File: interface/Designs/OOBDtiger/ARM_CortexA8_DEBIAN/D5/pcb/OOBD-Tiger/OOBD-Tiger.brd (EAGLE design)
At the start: 63.4 x 38.2 mm, 83 parts, among them IC4 DS3231, U1 SY6280, U10 MP1482DS, U2 SN65HVD230(SO8), U6 SN65HVD230(SO8)

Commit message: modify USB-OTG and USB-Host interface
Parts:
- added C2: 100nF, rcl:C0603
- added R19: 6k8k/1%, rcl:R0603
- added R21: 10k, rcl:R0603
- added R22: 2.2k/1%, rcl:R0603
- added R23: NA, rcl:R0603
- added R24: 10k/1%, rcl:R0603
- added U3: SY6280, OLIMEX_IC:SOT23-5
- renumbered USB_HOST2 to USB_HOST
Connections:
- net USB0-DRV renamed USB0_DRV
- net USB0-ID renamed USB0_ID
- net USB0-VBUS renamed USB0_VBUS
- removed net USB1_DM1: USB_HOST.2
- removed net USB1_DP1: USB_HOST.3
- removed net USB1_VBUS1: C10.1, C8.1, L5.1
- new net N$13: C10.1, C8.1, L5.1, R22.2, U3.1
- new net N$3: R19.2, U3.3
- net +5V: now also C2.1, U3.5
- net GND: now also C2.2, R19.1, R21.1, R24.1, U3.2
- net USB1_CE: now also R23.2
- net USB1_DM: now also USB_HOST.2
- net USB1_DP: now also USB_HOST.3
- net USB1_DRV: now also R21.2, R23.1, U3.4
- net USB1_ID: now also R24.2
- net USB1_VBUS: now also R22.1
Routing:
- net USB1_VBUS1: track 10.1 -> 0.00 mm, vias 2 -> 0
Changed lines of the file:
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@@
 <?xml version="1.0" encoding="utf-8"?>
 <!DOCTYPE eagle SYSTEM "eagle.dtd">
-<eagle version="7.6.0">
+<eagle version="6.4">
 <drawing>
 <settings>
@@
 <pass name="Default">
 <param name="RoutingGrid" value="50mil"/>
-<param name="AutoGrid" value="1"/>
-<param name="Efforts" value="0"/>
-<param name="TopRouterVariant" value="1"/>
 <param name="tpViaShape" value="round"/>
 <param name="PrefDir.1" value="|"/>
@@
 <element name="IC4" library="DS3231_industrialberry" package="SOIC-16W" value="DS3231" x="16.129" y="16.002" rot="R270"/>
 <element name="BAT2" library="SparkFun" package="BATTCON_12MM_PTH" value="" x="21.844" y="31.623"/>
-<element name="USB_HOST2" library="OLIMEX_CONNECTORS" package="USB_PN87520_DEV_PTH" value="USB_A_VERTICAL" x="2.159" y="16.129" rot="R270"/>
+<element name="USB_HOST" library="OLIMEX_CONNECTORS" package="USB_PN87520_DEV_PTH" value="USB_A_VERTICAL" x="2.159" y="16.129" rot="R270"/>
 <element name="L5" library="rcl" package="L0805_5MIL_DWS" value="FB0805/600R/2A" x="25.4" y="12.319" smashed="yes">
 <attribute name="NAME" x="27.305" y="11.811" size="1.27" layer="25" ratio="20"/>
@@
 <element name="MS-CAN" library="SparkFun" package="SJ_2S-NO" value="OPEN" x="1.778" y="6.731" rot="R180"/>
 <element name="R20" library="rcl" package="R0603" value="10k" x="14.351" y="27.686" rot="R90"/>
+<element name="C2" library="rcl" package="C0603" value="100nF" x="1.016" y="-2.794"/>
+<element name="U3" library="OLIMEX_IC" package="SOT23-5" value="SY6280" x="-5.461" y="-3.937"/>
+<element name="R19" library="rcl" package="R0603" value="6k8k/1%" x="-6.985" y="-14.859"/>
+<element name="R21" library="rcl" package="R0603" value="10k" x="1.397" y="-14.859"/>
+<element name="R22" library="rcl" package="R0603" value="2.2k/1%" x="-6.985" y="-10.033"/>
+<element name="R23" library="rcl" package="R0603" value="NA" x="-6.985" y="-19.685"/>
+<element name="R24" library="rcl" package="R0603" value="10k/1%" x="-6.985" y="-24.511"/>
 </elements>
 <signals>
@@
 <contactref element="IC4" pad="9"/>
 <contactref element="C3" pad="2"/>
-<contactref element="USB_HOST2" pad="4"/>
+<contactref element="USB_HOST" pad="4"/>
 <contactref element="C8" pad="2"/>
 <contactref element="C10" pad="2"/>
@@
 <via x="27.6225" y="20.955" extent="1-16" drill="0.3"/>
 <via x="33.9725" y="20.955" extent="1-16" drill="0.3"/>
+<contactref element="U3" pad="2"/>
+<contactref element="C2" pad="2"/>
+<contactref element="U3" pad="2"/>
+<contactref element="R19" pad="1"/>
+<contactref element="R21" pad="1"/>
+<contactref element="R24" pad="1"/>
+<wire x1="-7.835" y1="-14.859" x2="-7.835" y2="-24.511" width="0" layer="19" extent="1-1"/>
+<wire x1="0.547" y1="-14.859" x2="-7.835" y2="-14.859" width="0" layer="19" extent="1-1"/>
+<wire x1="-4.1609" y1="-3.937" x2="-7.835" y2="-14.859" width="0" layer="19" extent="1-1"/>
+<wire x1="1.866" y1="-2.794" x2="-4.1609" y2="-3.937" width="0" layer="19" extent="1-1"/>
+<wire x1="3.81" y1="2.159" x2="1.866" y2="-2.794" width="0" layer="19" extent="1-1"/>
 </signal>
 <signal name="VCC" class="1">
@@
 <via x="32.7025" y="8.255" extent="1-16" drill="0.3"/>
 <via x="32.7025" y="25.0825" extent="1-16" drill="0.3"/>
+<contactref element="C2" pad="1"/>
+<contactref element="U3" pad="5"/>
+<wire x1="0.166" y1="-2.794" x2="27.94" y2="6.223" width="0" layer="19" extent="1-1"/>
+<wire x1="-6.7611" y1="-4.887" x2="0.166" y2="-2.794" width="0" layer="19" extent="1-1"/>
 </signal>
 <signal name="USB0_DP">
@@
 <via x="9.2075" y="31.115" extent="1-16" drill="0.3"/>
 </signal>
-<signal name="USB0-DRV">
+<signal name="USB0_DRV">
 <contactref element="U1" pad="4"/>
 <contactref element="R4" pad="2"/>
@@
 <via x="30.7975" y="25.7175" extent="1-16" drill="0.3"/>
 </signal>
-<signal name="USB0-VBUS">
+<signal name="USB0_VBUS">
 <contactref element="R1" pad="1"/>
 <contactref element="AM3352-SOM-EVB-PLATFORM" pad="3-11"/>
@@
 <via x="43.815" y="3.4925" extent="1-16" drill="0.3"/>
 </signal>
-<signal name="USB0-ID">
+<signal name="USB0_ID">
 <contactref element="USB_OTG" pad="ID"/>
 <contactref element="AM3352-SOM-EVB-PLATFORM" pad="3-12"/>
@@
 <signal name="USB1_ID">
 <contactref element="AM3352-SOM-EVB-PLATFORM" pad="3-6"/>
+<contactref element="R24" pad="2"/>
+<wire x1="-6.135" y1="-24.511" x2="57.15" y2="2.159" width="0" layer="19" extent="1-1"/>
 </signal>
 <signal name="PMIC_POWER_EN">
@@
 <signal name="USB1_DP">
 <contactref element="AM3352-SOM-EVB-PLATFORM" pad="3-7"/>
+<contactref element="USB_HOST" pad="3"/>
+<wire x1="4.869" y1="17.129" x2="55.88" y2="6.223" width="0" layer="19" extent="1-1"/>
 </signal>
 <signal name="USB1_DM">
 <contactref element="AM3352-SOM-EVB-PLATFORM" pad="3-9"/>
+<contactref element="USB_HOST" pad="2"/>
+<wire x1="4.869" y1="15.129" x2="54.61" y2="6.223" width="0" layer="19" extent="1-1"/>
 </signal>
 <signal name="USB1_VBUS">
 <contactref element="AM3352-SOM-EVB-PLATFORM" pad="3-5"/>
+<contactref element="R22" pad="1"/>
+<wire x1="-7.835" y1="-10.033" x2="57.15" y2="6.223" width="0" layer="19" extent="1-1"/>
 </signal>
 <signal name="USB1_DRV">
 <contactref element="AM3352-SOM-EVB-PLATFORM" pad="3-10"/>
+<contactref element="U3" pad="4"/>
+<contactref element="R21" pad="2"/>
+<contactref element="R23" pad="1"/>
+<wire x1="2.247" y1="-14.859" x2="54.61" y2="2.159" width="0" layer="19" extent="1-1"/>
+<wire x1="-7.835" y1="-19.685" x2="2.247" y2="-14.859" width="0" layer="19" extent="1-1"/>
+<wire x1="-6.7611" y1="-2.987" x2="2.247" y2="-14.859" width="0" layer="19" extent="1-1"/>
 </signal>
 <signal name="USB1_CE">
 <contactref element="AM3352-SOM-EVB-PLATFORM" pad="3-8"/>
+<contactref element="R23" pad="2"/>
+<wire x1="-6.135" y1="-19.685" x2="55.88" y2="2.159" width="0" layer="19" extent="1-1"/>
 </signal>
 <signal name="USB0_CE">
@@
 </signal>
 <signal name="N$28">
-<contactref element="USB_HOST2" pad="1"/>
+<contactref element="USB_HOST" pad="1"/>
 <contactref element="L5" pad="2"/>
 <contactref element="C3" pad="1"/>
@@
 <via x="27.6225" y="14.605" extent="1-16" drill="0.3"/>
 </signal>
-<signal name="USB1_DP1">
-<contactref element="USB_HOST2" pad="3"/>
-</signal>
-<signal name="USB1_DM1">
-<contactref element="USB_HOST2" pad="2"/>
-</signal>
-<signal name="USB1_VBUS1">
-<contactref element="L5" pad="1"/>
-<contactref element="C8" pad="1"/>
-<contactref element="C10" pad="1"/>
-<wire x1="23.495" y1="17.78" x2="24.257" y2="17.018" width="0.127" layer="1"/>
-<wire x1="23.495" y1="19.05" x2="23.495" y2="17.78" width="0.127" layer="1"/>
-<wire x1="24.257" y1="19.812" x2="23.495" y2="19.05" width="0.127" layer="1"/>
-<wire x1="25.0825" y1="13.0175" x2="24.384" y2="12.319" width="0.127" layer="1"/>
-<wire x1="25.0825" y1="13.335" x2="25.0825" y2="13.0175" width="0.127" layer="1"/>
-<wire x1="25.4" y1="13.6525" x2="25.0825" y2="13.335" width="0.127" layer="1"/>
-<wire x1="25.4" y1="15.5575" x2="25.4" y2="13.6525" width="0.127" layer="1"/>
-<wire x1="25.0825" y1="15.875" x2="25.4" y2="15.5575" width="0.127" layer="16"/>
-<wire x1="23.8125" y1="15.875" x2="25.0825" y2="15.875" width="0.127" layer="16"/>
-<wire x1="24.13" y1="16.1925" x2="23.8125" y2="15.875" width="0.127" layer="1"/>
-<wire x1="24.13" y1="16.8275" x2="24.13" y2="16.1925" width="0.127" layer="1"/>
-<wire x1="24.13" y1="16.8275" x2="24.257" y2="17.018" width="0.127" layer="1"/>
-<via x="25.4" y="15.5575" extent="1-16" drill="0.3"/>
-<via x="23.8125" y="15.875" extent="1-16" drill="0.3"/>
-</signal>
 <signal name="N$29">
-<contactref element="USB_HOST2" pad="P$1"/>
-<contactref element="USB_HOST2" pad="P$2"/>
+<contactref element="USB_HOST" pad="P$1"/>
+<contactref element="USB_HOST" pad="P$2"/>
 <contactref element="L6" pad="2"/>
 <wire x1="25.7175" y1="13.6525" x2="26.416" y2="14.351" width="0.127" layer="1"/>
@@
 <wire x1="1.328" y1="6.731" x2="40.894" y2="16.344" width="0" layer="19" extent="1-1"/>
 </signal>
+<signal name="N$3">
+<contactref element="U3" pad="3"/>
+<contactref element="R19" pad="2"/>
+<wire x1="-4.1609" y1="-2.987" x2="-6.135" y2="-14.859" width="0" layer="19" extent="1-1"/>
+</signal>
+<signal name="N$13">
+<contactref element="R22" pad="2"/>
+<contactref element="U3" pad="1"/>
+<contactref element="L5" pad="1"/>
+<contactref element="C8" pad="1"/>
+<contactref element="C10" pad="1"/>
+<wire x1="24.257" y1="17.018" x2="24.257" y2="19.812" width="0" layer="19" extent="1-1"/>
+<wire x1="24.384" y1="12.319" x2="24.257" y2="17.018" width="0" layer="19" extent="1-1"/>
+<wire x1="-4.1609" y1="-4.887" x2="24.384" y2="12.319" width="0" layer="19" extent="1-1"/>
+<wire x1="-6.135" y1="-10.033" x2="-4.1609" y2="-4.887" width="0" layer="19" extent="1-1"/>
+</signal>
 </signals>

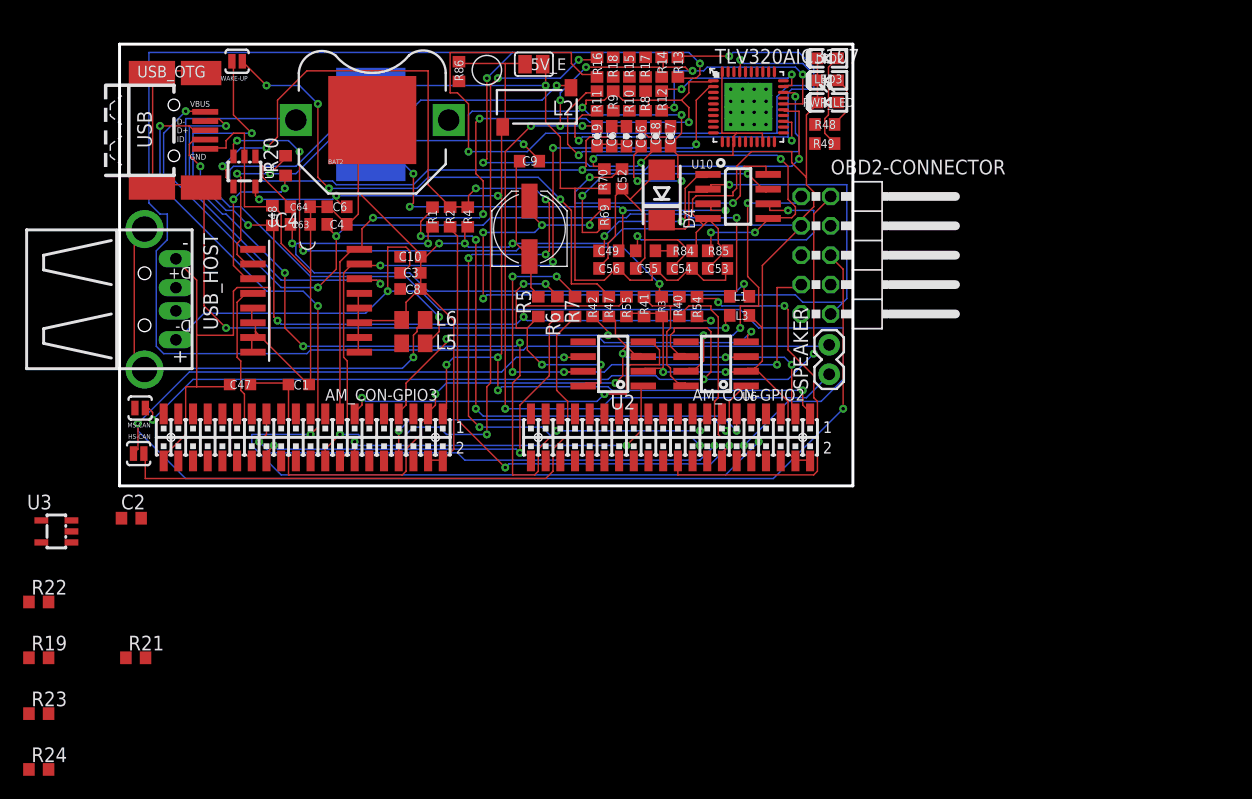
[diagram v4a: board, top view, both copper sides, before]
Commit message: ISO1050 wieder entfernt, ADM3053 hinzugefügt, optional als Jumper
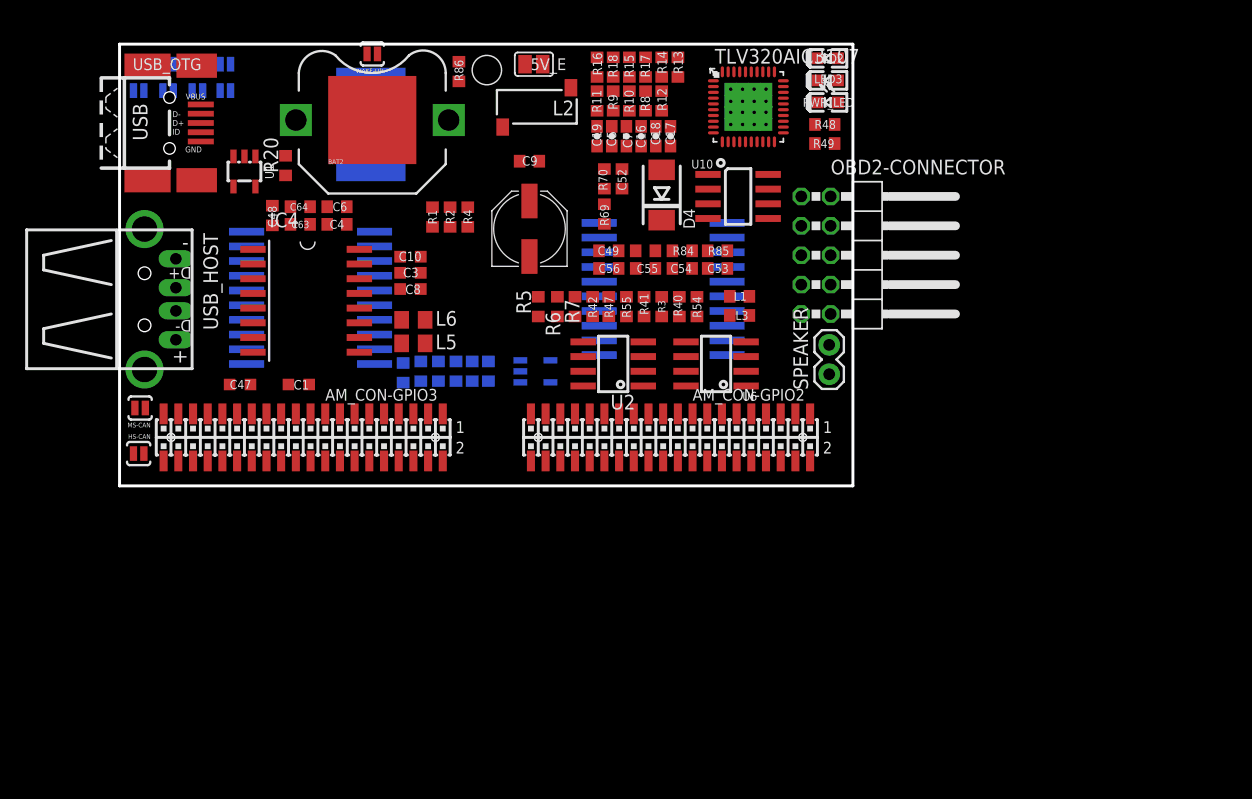
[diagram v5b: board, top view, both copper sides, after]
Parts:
- added HS-CAN_H-DISABLE, HS-CAN_L-DISABLE, MS-CAN_H-DISABLE, MS-CAN_L-DISABLE: CLOSED, SparkFun:SJ_2S-NO
- added HS-CAN_H-ENABLE, HS-CAN_L-ENABLE, MS-CAN_H-ENABLE, MS-CAN_L-ENABLE: OPEN (use jumper), SparkFun:SJ_2S-NO
- added IC1, IC2: ADM3053M, ADM3053:SO20W
- moved R24 51.9 mm to (31.9, 9.91), flipped to the bottom, turned to 90 degrees
- moved R23 47.7 mm to (30.5, 9.91), flipped to the bottom, turned to 90 degrees
- moved U3 43.7 mm to (35.9, 9.91), flipped to the bottom
- moved R19 42.5 mm to (27.6, 9.91), flipped to the bottom, turned to 90 degrees
- moved R22 38.6 mm to (26.0, 9.91), flipped to the bottom, turned to 90 degrees
- moved R21 37.1 mm to (29.1, 9.91), flipped to the bottom, turned to 90 degrees
- moved C2 26.6 mm to (24.5, 9.78), flipped to the bottom, turned to 90 degrees
- moved WAKE-UP 11.7 mm to (21.8, 37.3)
- moved USB_OTG 0.74 mm to (4.32, 31.4)
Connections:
- new net GND1: IC1.1, IC1.10, IC1.3, IC1.7, IC1.9, IC2.1, IC2.10, IC2.3, IC2.7, IC2.9
- new net GND2: IC1.11, IC1.13, IC1.16, IC1.20, IC2.11, IC2.13, IC2.16, IC2.20
- new net N$30: HS-CAN_L-DISABLE.2, R6.2, U2.7
- new net N$31: HS-CAN_H-DISABLE.2, HS-CAN_L-ENABLE.2, OBD2-CONNECTOR.6
- new net N$32: IC2.15, MS-CAN_L-ENABLE.2
- new net N$33: MS-CAN_H-DISABLE.2, R42.2, U6.7
- new net N$34: HS-CAN_H-ENABLE.1, IC1.17
- new net N$35: HS-CAN_L-ENABLE.1, IC1.15
- new net N$36: MS-CAN_L-DISABLE.1, MS-CAN_L-ENABLE.1, OBD2-CONNECTOR.2
- new net N$37: MS-CAN_H-DISABLE.1, MS-CAN_H-ENABLE.2, OBD2-CONNECTOR.1
- new net V_IO: IC1.6, IC2.6
- net CANH: now also IC2.17, MS-CAN_H-ENABLE.1; no longer OBD2-CONNECTOR.1, R42.2, U6.7
- net CANH1: now also HS-CAN_H-ENABLE.2, HS-CAN_L-DISABLE.1; no longer R6.2, U2.7
- net CANL: now also MS-CAN_L-DISABLE.2; no longer OBD2-CONNECTOR.2
- net CANL1: now also HS-CAN_H-DISABLE.1; no longer OBD2-CONNECTOR.6
- net VCC: now also IC1.8, IC2.8
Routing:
- net GND: track 302.2 -> 0.00 mm, vias 5 -> 0
- net N$15: track 163.2 -> 0.00 mm, vias 4 -> 0
- net CANL1: track 123.1 -> 0.00 mm, vias 3 -> 0
- net +3V3: track 98.0 -> 0.00 mm, vias 7 -> 0
- net N$17: track 96.6 -> 0.00 mm, vias 3 -> 0
- net USB0_DP: track 96.4 -> 0.00 mm, vias 4 -> 0
- net +5V: track 96.2 -> 0.00 mm, vias 7 -> 0
- net USB0_DRV: track 95.8 -> 0.00 mm, vias 8 -> 0
- net CANL: track 86.6 -> 0.00 mm, vias 3 -> 0
- net +12V: track 83.5 -> 0.00 mm, vias 5 -> 0
- net USB0_ID: track 82.7 -> 0.00 mm, vias 2 -> 0
- net N$44: track 82.5 -> 0.00 mm, vias 5 -> 0
- net USB0_DM: track 79.8 -> 0.00 mm, vias 6 -> 0
- net N$266: track 76.4 -> 0.00 mm, vias 2 -> 0
- net VCC: track 75.0 -> 0.00 mm, vias 5 -> 0
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
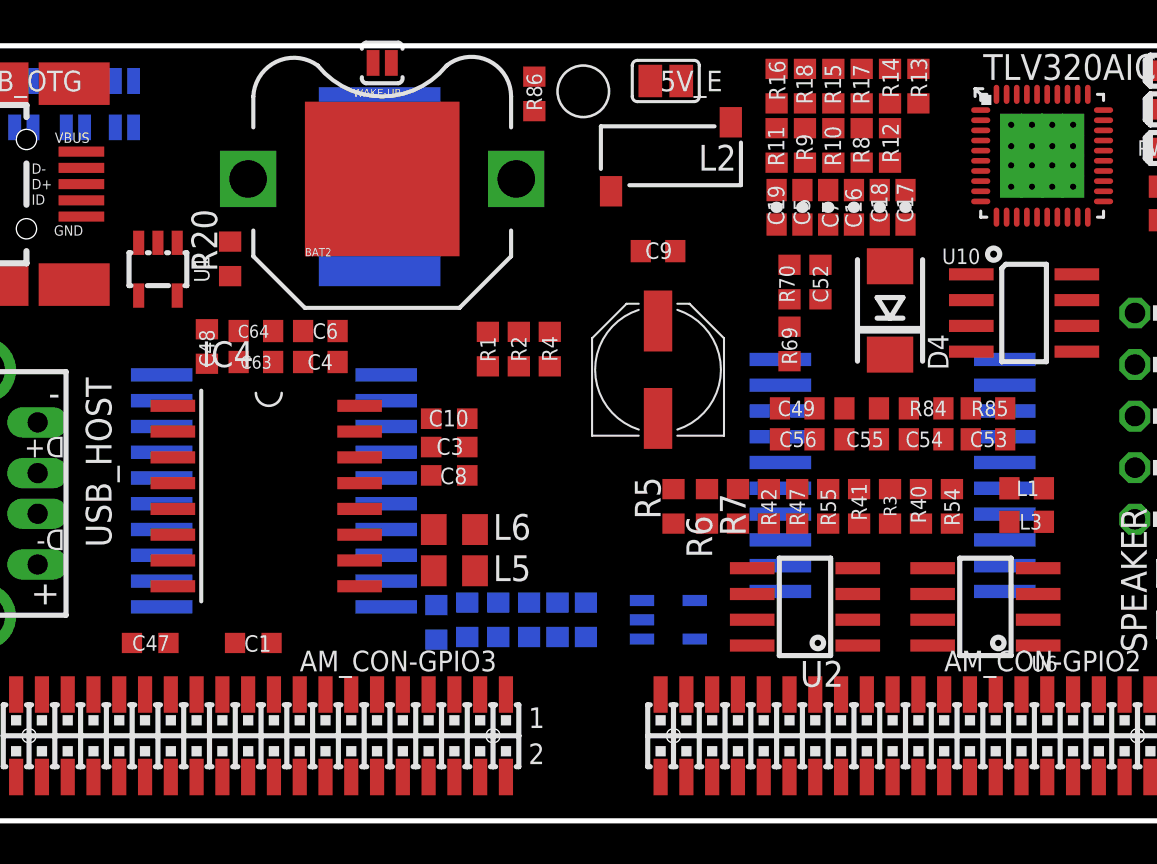
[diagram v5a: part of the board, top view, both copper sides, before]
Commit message: ADM3053 mit Beschallung gesehen und auf dem PCB platziert.
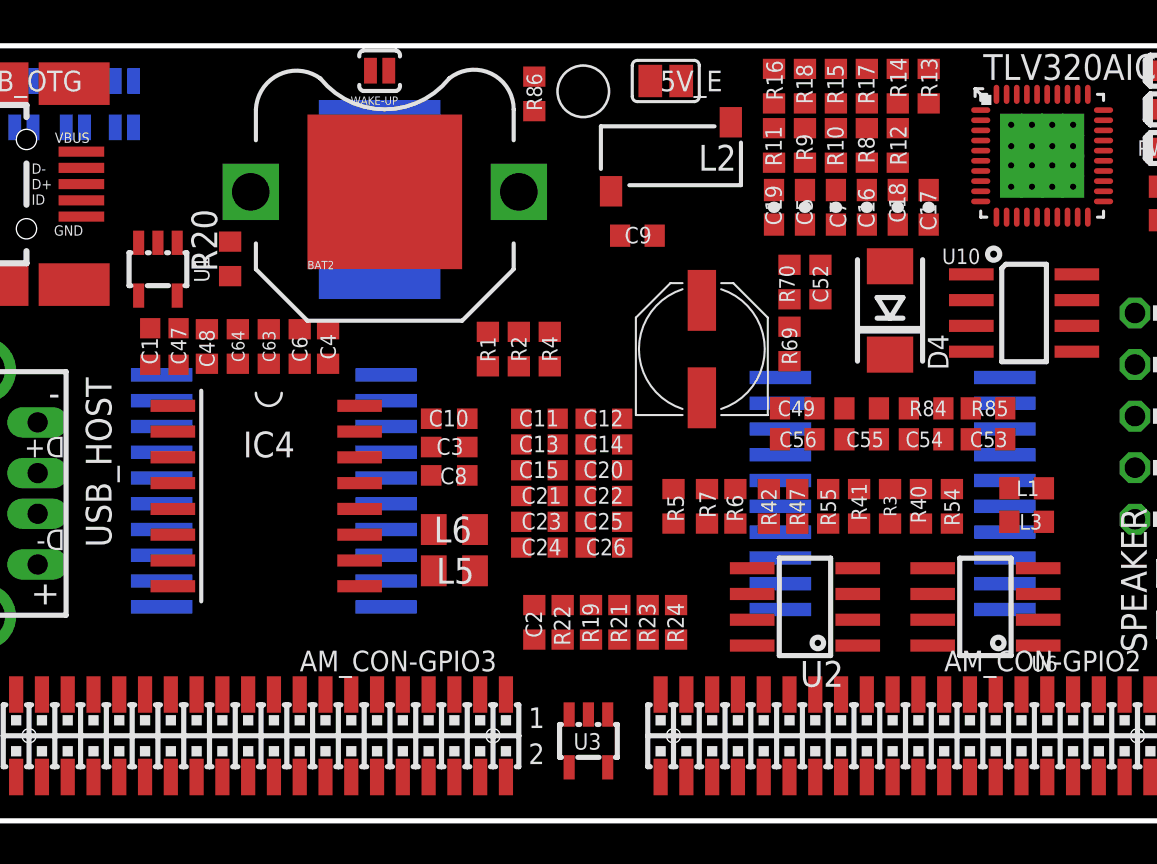
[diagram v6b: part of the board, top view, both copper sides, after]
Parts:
- added C11, C13, C15, C21, C23, C25: 100nF, rcl:C0603_OLIMEX
- added C12, C14, C20, C22, C24, C26: 10µF, rcl:C0603_OLIMEX
- moved C1 15.5 mm to (10.4, 23.4), turned to 270 degrees
- moved C47 14.7 mm to (11.8, 23.4), turned to 270 degrees
- moved U3 7.15 mm to (32.0, 3.94), flipped to the top, turned to 90 degrees
- moved C2 4.83 mm to (29.3, 9.78), flipped to the top
- moved R22 4.70 mm to (30.7, 9.78), flipped to the top
- moved R19 4.57 mm to (32.1, 9.78), flipped to the top
- moved R24 4.45 mm to (36.3, 9.78), flipped to the top
- moved R21 4.45 mm to (33.5, 9.78), flipped to the top
- moved R23 4.45 mm to (34.9, 9.78), flipped to the top
- moved C51 2.39 mm to (37.6, 23.2)
- moved C6 1.27 mm to (17.8, 23.4), turned to 270 degrees
- moved C9 1.27 mm to (34.4, 28.8)
- moved C64 1.17 mm to (14.7, 23.4), turned to 90 degrees
- moved C17 1.14 mm to (48.8, 30.2)
- moved C63 0.99 mm to (16.3, 23.4), turned to 90 degrees
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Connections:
- removed net GND2: IC1.11, IC1.13, IC1.16, IC1.20, IC2.11, IC2.13, IC2.16, IC2.20
- removed net V_IO: IC1.6, IC2.6
- new net N$38: IC2.11, IC2.13, IC2.14, IC2.16
- new net N$39: IC2.6
- new net N$40: IC1.19
- new net N$41: IC1.12
- new net N$42: IC2.10, IC2.20, IC2.9
- new net N$45: IC1.11, IC1.13, IC1.14, IC1.16
- new net N$46: IC1.10, IC1.20
- net +5V: now also C11.1, C12.1, C13.1, C14.1, C15.1, C20.1, C21.1, C22.1, C23.1, C24.1, C25.1, C26.1, IC1.6, IC1.8, IC2.12, IC2.19, IC2.8
- net GND: now also C11.2, C12.2, C13.2, C14.2, C15.2, C20.2, C21.2, C22.2, C23.2, C24.2, C25.2, C26.2, IC1.1, IC1.3, IC1.7, IC2.1, IC2.3, IC2.7
- net GND1: no longer IC1.1, IC1.10, IC1.3, IC1.7, IC2.1, IC2.10, IC2.3, IC2.7, IC2.9
- net VCC: no longer IC1.8, IC2.8
